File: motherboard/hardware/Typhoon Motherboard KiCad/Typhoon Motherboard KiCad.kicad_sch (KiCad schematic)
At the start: 2 parts, among them P1 USB_C_Plug_USB2.0, U1 ESP32-S3-WROOM-1

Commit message: added most recent motherboard files
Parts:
- added R1, R2: 22, symbol Device:R_US
- added U2: CP2102N-Axx-xQFN20, Package_DFN_QFN:SiliconLabs_QFN-20-1EP_3x3mm_P0.5mm, symbol Interface_USB:CP2102N-Axx-xQFN20
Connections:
- net GND: now reaches U1.1 (GND), U1.40 (GND), U1.41 (GND)
- net GND: now also P1.A1 (GND), P1.A12 (GND), P1.B1 (GND), P1.B12 (GND)
- net +3.3V: now reaches U1.2 (3V3)
- net at U1.36 (RXD0): now also U2.17 (RXD)
- net at U1.37 (TXD0): now also U2.18 (TXD)
- net +5V: now reaches P1.A4 (VBUS), P1.A9 (VBUS), P1.B4 (VBUS), P1.B9 (VBUS)
- net at P1.A6 (D+): now also R2.1
- net at P1.A7 (D-): now also R1.1
- new net: R1.2, U2.5 (D-)
- new net: R2.2, U2.4 (D+)
- new net: U2.12 (GND), U2.21 (GND), U2.3 (GND)
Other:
- note added: "3.3V"
- moved on the sheet: P1

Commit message: Minor Changes
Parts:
- added J1: Conn_01x01_Pin, symbol Connector:Conn_01x01_Pin
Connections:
- net +3.3V: no longer names the net of U1.2 (3V3)
- net +3.3V: now also J1.1 (Pin_1)
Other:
- note removed: "3.3V"
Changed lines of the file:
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@@
+	(wire
+		(pts
+			(xy 194.31 50.8) (xy 194.31 59.69)
+		)
+		(stroke
+			(width 0)
+			(type default)
+		)
+	)
 	(wire
 		(pts
@@
 			(width 0)
 			(type default)
-		)
-	)
-	(text "3.3V"
-		(exclude_from_sim no)
-		(at 189.992 56.134 0)
-		(effects
-			(font
-				(size 1.27 1.27)
-			)
 		)
 	)
@@
 	)
 	(symbol
-		(lib_id "power:+3.3V")
-		(at 194.31 59.69 0)
-		(unit 1)
-		(exclude_from_sim no)
-		(in_bom yes)
-		(on_board yes)
-		(dnp no)
-		(fields_autoplaced yes)
-		(property "Reference" "#PWR01"
-			(at 194.31 63.5 0)
-			(effects
-				(font
-					(size 1.27 1.27)
-				)
-				(hide yes)
-			)
-		)
-		(property "Value" "+3.3V"
-			(at 194.31 54.61 0)
-			(effects
-				(font
-					(size 1.27 1.27)
-				)
-			)
-		)
-		(property "Footprint" ""
-			(at 194.31 59.69 0)
-			(effects
-				(font
-					(size 1.27 1.27)
-				)
-				(hide yes)
-			)
-		)
-		(property "Datasheet" ""
-			(at 194.31 59.69 0)
-			(effects
-				(font
-					(size 1.27 1.27)
-				)
-				(hide yes)
-			)
-		)
-		(property "Description" "Power symbol creates a global label with name \"+3.3V\""
-			(at 194.31 59.69 0)
-			(effects
-				(font
-					(size 1.27 1.27)
-				)
-				(hide yes)
-			)
-		)
-		(pin "1"
-		)
-		(instances
-			(project "Typhoon Motherboard KiCad"
-				(path "/13012fcd-02e9-4b82-8301-52da00f60a6e"
-					(reference "#PWR01")
-					(unit 1)
-				)
-			)
-		)
-	)
-	(symbol
 		(lib_id "power:GND")
 		(at 97.79 104.14 0)
@@
 					(unit 1)
 				)
+			)
+		)
+	)
+	(symbol
+		(lib_id "Connector:Conn_01x01_Pin")
+		(at 189.23 50.8 0)
+		(unit 1)
+		(exclude_from_sim no)
+		(in_bom yes)
+		(on_board yes)
+		(dnp no)
+		(fields_autoplaced yes)
+		(property "Reference" "J1"
+			(at 189.865 45.72 0)
+			(effects
+				(font
+					(size 1.27 1.27)
+				)
+			)
+		)
+		(property "Value" "Conn_01x01_Pin"
+			(at 189.865 48.26 0)
+			(effects
+				(font
+					(size 1.27 1.27)
+				)
+			)
+		)
+		(property "Footprint" ""
+			(at 189.23 50.8 0)
+			(effects
+				(font
+					(size 1.27 1.27)
+				)
+				(hide yes)
+			)
+		)
+		(property "Datasheet" "~"
+			(at 189.23 50.8 0)
+			(effects
+				(font
+					(size 1.27 1.27)
+				)
+				(hide yes)
+			)
+		)
+		(property "Description" "Generic connector, single row, 01x01, script generated"
+			(at 189.23 50.8 0)
+			(effects
+				(font
+					(size 1.27 1.27)
+				)
+				(hide yes)
+			)
+		)
+		(pin "1"
+		)
+		(instances
+			(project "Typhoon Motherboard KiCad"
+				(path "/13012fcd-02e9-4b82-8301-52da00f60a6e"
+					(reference "J1")
+					(unit 1)
+				)

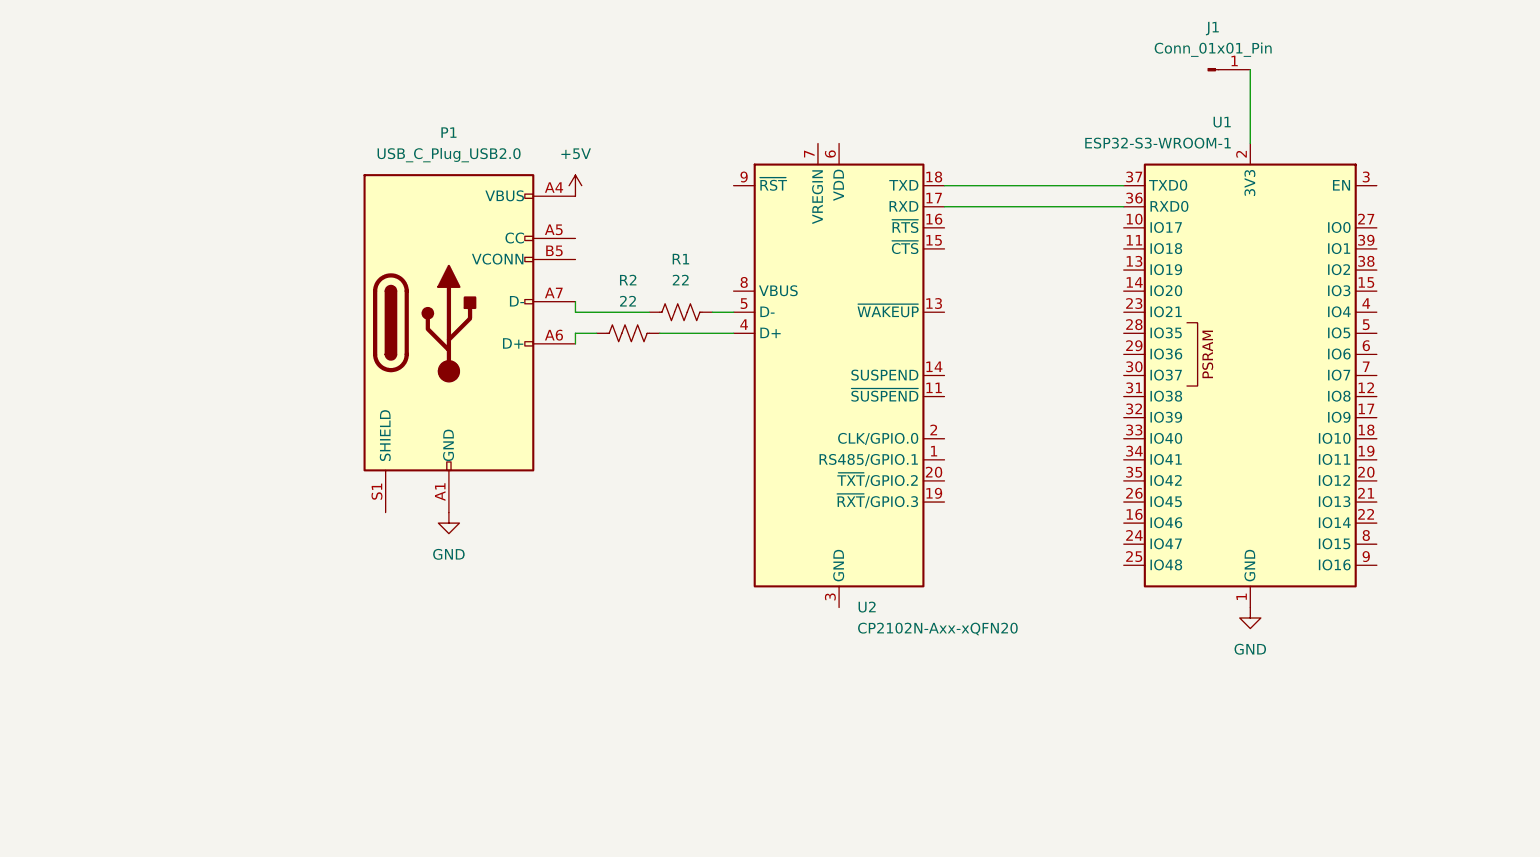
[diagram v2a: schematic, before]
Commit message: Removed  UART
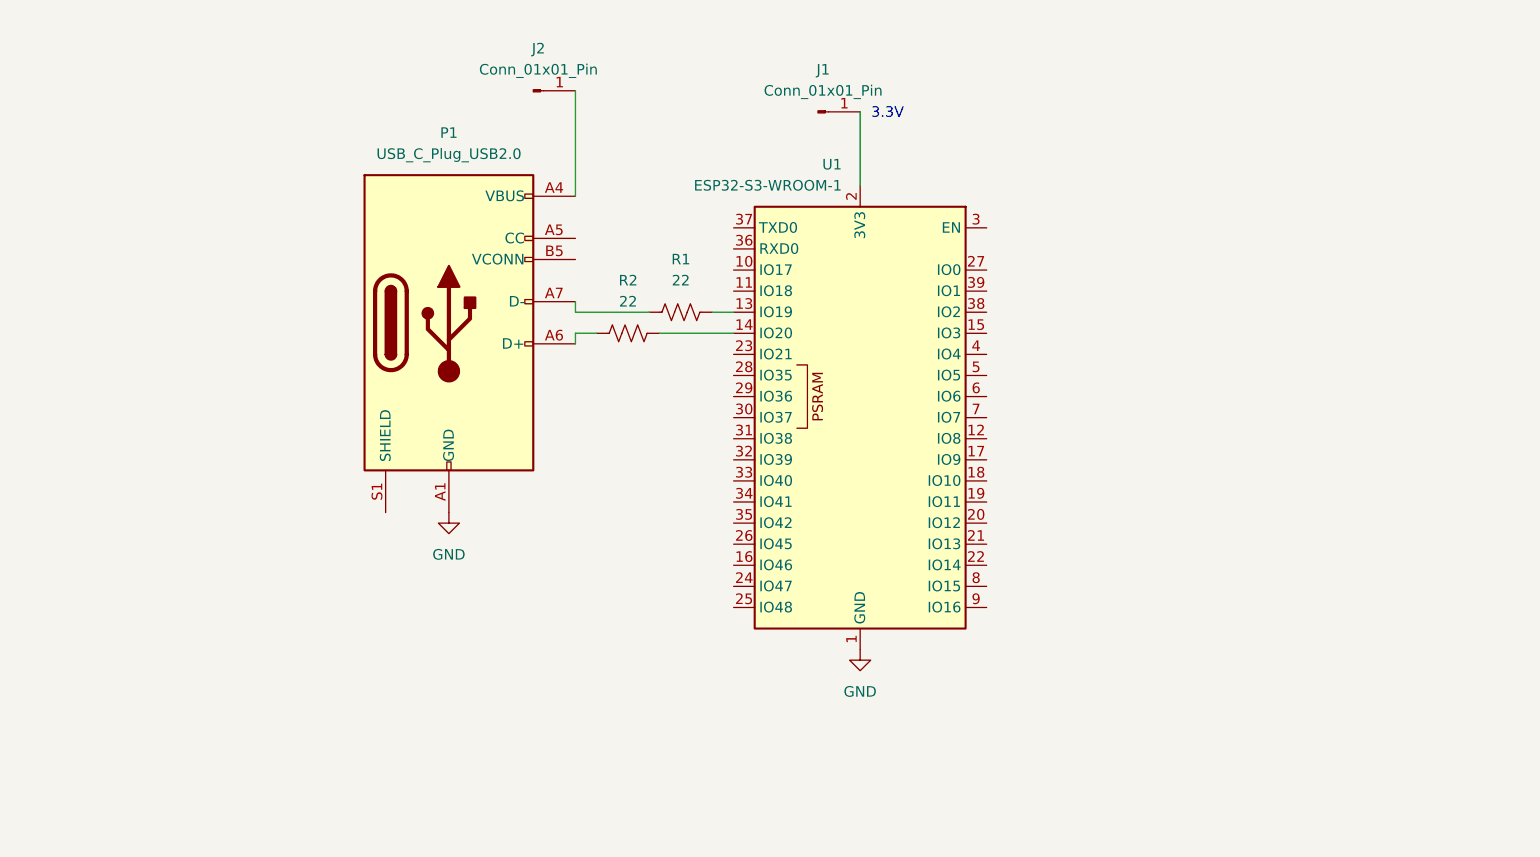
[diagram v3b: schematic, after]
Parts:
- removed U2: CP2102N-Axx-xQFN20, Package_DFN_QFN:SiliconLabs_QFN-20-1EP_3x3mm_P0.5mm, symbol Interface_USB:CP2102N-Axx-xQFN20
- added J2: Conn_01x01_Pin, symbol Connector:Conn_01x01_Pin
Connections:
- net at R1.2: now also U1.13 (IO19)
- net at R2.2: now also U1.14 (IO20)
- net +5V: no longer names the net of P1.A4 (VBUS), P1.A9 (VBUS), P1.B4 (VBUS), P1.B9 (VBUS)
- net +5V: now also J2.1 (Pin_1)
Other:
- note added: "3.3V"
- moved on the sheet: J1, U1
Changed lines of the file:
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@@
 	(wire
 		(pts
-			(xy 194.31 50.8) (xy 194.31 59.69)
-		)
-		(stroke
-			(width 0)
-			(type default)
-		)
-	)
-	(wire
-		(pts
-			(xy 179.07 64.77) (xy 157.48 64.77)
+			(xy 147.32 55.88) (xy 147.32 64.77)
+		)
+		(stroke
+			(width 0)
+			(type default)
+		)
+	)
+	(wire
+		(pts
+			(xy 113.03 53.34) (xy 113.03 66.04)
 		)
 		(stroke
@@
 	(wire
 		(pts
-			(xy 179.07 67.31) (xy 157.48 67.31)
-		)
-		(stroke
-			(width 0)
-			(type default)
-		)
-	)
-	(wire
-		(pts
 			(xy 132.08 80.01) (xy 129.54 80.01)
 		)
@@
 			(width 0)
 			(type default)
+		)
+	)
+	(text "3.3V"
+		(exclude_from_sim no)
+		(at 150.622 56.134 0)
+		(effects
+			(font
+				(size 1.27 1.27)
+			)
+		)
+	)
+	(symbol
+		(lib_id "Connector:Conn_01x01_Pin")
+		(at 107.95 53.34 0)
+		(unit 1)
+		(exclude_from_sim no)
+		(in_bom yes)
+		(on_board yes)
+		(dnp no)
+		(fields_autoplaced yes)
+		(property "Reference" "J2"
+			(at 108.585 48.26 0)
+			(effects
+				(font
+					(size 1.27 1.27)
+				)
+			)
+		)
+		(property "Value" "Conn_01x01_Pin"
+			(at 108.585 50.8 0)
+			(effects
+				(font
+					(size 1.27 1.27)
+				)
+			)
+		)
+		(property "Footprint" ""
+			(at 107.95 53.34 0)
+			(effects
+				(font
+					(size 1.27 1.27)
+				)
+				(hide yes)
+			)
+		)
+		(property "Datasheet" "~"
+			(at 107.95 53.34 0)
+			(effects
+				(font
+					(size 1.27 1.27)
+				)
+				(hide yes)
+			)
+		)
+		(property "Description" "Generic connector, single row, 01x01, script generated"
+			(at 107.95 53.34 0)
+			(effects
+				(font
+					(size 1.27 1.27)
+				)
+				(hide yes)
+			)
+		)
+		(pin "1"
+		)
+		(instances
+			(project "Typhoon Motherboard KiCad"
+				(path "/13012fcd-02e9-4b82-8301-52da00f60a6e"
+					(reference "J2")
+					(unit 1)
+				)
+			)
 		)
 	)
@@
 	(symbol
 		(lib_id "RF_Module:ESP32-S3-WROOM-1")
-		(at 194.31 87.63 0)
+		(at 147.32 92.71 0)
 		(mirror y)
 		(unit 1)
@@
 		(dnp no)
 		(property "Reference" "U1"
-			(at 192.1159 57.15 0)
+			(at 145.1259 62.23 0)
 			(effects
 				(font
@@
 		)
 		(property "Value" "ESP32-S3-WROOM-1"
-			(at 192.1159 59.69 0)
+			(at 145.1259 64.77 0)
 			(effects
 				(font
@@
 		)
 		(property "Footprint" "RF_Module:ESP32-S3-WROOM-1"
-			(at 194.31 85.09 0)
+			(at 147.32 90.17 0)
 			(effects
 				(font
@@
 		)
 		(property "Datasheet" "https://www.espressif.com/sites/default/files/documentation/esp32-s3-wroom-1_wroom-1u_datasheet_en.pdf"
-			(at 194.31 87.63 0)
+			(at 147.32 92.71 0)
 			(effects
 				(font
@@
 		)
 		(property "Description" "RF Module, ESP32-S3 SoC, Wi-Fi 802.11b/g/n, Bluetooth, BLE, 32-bit, 3.3V, onboard antenna, SMD"
-			(at 194.31 87.63 0)
+			(at 147.32 92.71 0)
 			(effects
 				(font
@@
 	(symbol
 		(lib_id "power:GND")
-		(at 194.31 115.57 0)
+		(at 147.32 120.65 0)
 		(unit 1)
 		(exclude_from_sim no)
@@
 		(fields_autoplaced yes)
 		(property "Reference" "#PWR04"
-			(at 194.31 121.92 0)
+			(at 147.32 127 0)
 			(effects
 				(font
@@
 		)
 		(property "Value" "GND"
-			(at 194.31 120.65 0)
+			(at 147.32 125.73 0)
 			(effects
 				(font
@@
 		)
 		(property "Footprint" ""
-			(at 194.31 115.57 0)
+			(at 147.32 120.65 0)
 			(effects
 				(font
@@
 		)
 		(property "Datasheet" ""
-			(at 194.31 115.57 0)
+			(at 147.32 120.65 0)
 			(effects
 				(font
@@
 		)
 		(property "Description" "Power symbol creates a global label with name \"GND\" , ground"
-			(at 194.31 115.57 0)
+			(at 147.32 120.65 0)
 			(effects
 				(font
@@
 	)
 	(symbol
-		(lib_id "power:+5V")
-		(at 113.03 66.04 0)
-		(unit 1)
-		(exclude_from_sim no)
-		(in_bom yes)
-		(on_board yes)
-		(dnp no)
-		(property "Reference" "#PWR02"
-			(at 113.03 69.85 0)
-			(effects
-				(font
-					(size 1.27 1.27)
-				)
-				(hide yes)
-			)
-		)
-		(property "Value" "+5V"
-			(at 113.03 60.96 0)
-			(effects
-				(font
-					(size 1.27 1.27)
-				)
-			)
-		)
-		(property "Footprint" ""
-			(at 113.03 66.04 0)
-			(effects
-				(font
-					(size 1.27 1.27)
-				)
-				(hide yes)
-			)
-		)
-		(property "Datasheet" ""
-			(at 113.03 66.04 0)
-			(effects
-				(font
-					(size 1.27 1.27)
-				)
-				(hide yes)
-			)
-		)
-		(property "Description" "Power symbol creates a global label with name \"+5V\""
-			(at 113.03 66.04 0)
-			(effects
-				(font
-					(size 1.27 1.27)
-				)
-				(hide yes)
-			)
-		)
-		(pin "1"
-		)
-		(instances
-			(project "Typhoon Motherboard KiCad"
-				(path "/13012fcd-02e9-4b82-8301-52da00f60a6e"
-					(reference "#PWR02")
-					(unit 1)
-				)
-			)
-		)
-	)
-	(symbol
 		(lib_id "power:GND")
 		(at 97.79 104.14 0)
@@
 	)
 	(symbol
-		(lib_id "Interface_USB:CP2102N-Axx-xQFN20")
-		(at 144.78 87.63 0)
-		(unit 1)
-		(exclude_from_sim no)
-		(in_bom yes)
-		(on_board yes)
-		(dnp no)
-		(fields_autoplaced yes)
-		(property "Reference" "U2"
-			(at 146.9741 115.57 0)
-			(effects
-				(font
-					(size 1.27 1.27)
-				)
-				(justify left)
-			)
-		)
-		(property "Value" "CP2102N-Axx-xQFN20"
-			(at 146.9741 118.11 0)
-			(effects
-				(font
-					(size 1.27 1.27)
-				)
-				(justify left)
-			)
-		)
-		(property "Footprint" "Package_DFN_QFN:SiliconLabs_QFN-20-1EP_3x3mm_P0.5mm"
-			(at 176.53 114.3 0)
-			(effects
-				(font
-					(size 1.27 1.27)
-				)
-				(hide yes)
-			)
-		)
-		(property "Datasheet" "https://www.silabs.com/documents/public/data-sheets/cp2102n-datasheet.pdf"
-			(at 146.05 106.68 0)
-			(effects
-				(font
-					(size 1.27 1.27)
-				)
-				(hide yes)
-			)
-		)
-		(property "Description" "USB to UART master bridge, QFN-20"
-			(at 144.78 87.63 0)
-			(effects
-				(font
-					(size 1.27 1.27)
-				)
-				(hide yes)
-			)
-		)
-		(pin "1"
-		)
-		(pin "14"
-		)
-		(pin "15"
-		)
-		(pin "10"
-		)
-		(pin "11"
-		)
-		(pin "4"
-		)
-		(pin "5"
-		)
-		(pin "6"
-		)
-		(pin "21"
-		)
-		(pin "3"
-		)
-		(pin "16"
-		)
-		(pin "17"
-		)
-		(pin "18"
-		)
-		(pin "19"
-		)
-		(pin "7"
-		)
-		(pin "8"
-		)
-		(pin "9"
-		)
-		(pin "12"
-		)
-		(pin "13"
-		)
-		(pin "2"
-		)
-		(pin "20"
-		)
-		(instances
-			(project "Typhoon Motherboard KiCad"
-				(path "/13012fcd-02e9-4b82-8301-52da00f60a6e"
-					(reference "U2")
-					(unit 1)
-				)
-			)
-		)
-	)
-	(symbol
 		(lib_id "Connector:Conn_01x01_Pin")
-		(at 189.23 50.8 0)
+		(at 142.24 55.88 0)
 		(unit 1)
 		(exclude_from_sim no)
@@
 		(fields_autoplaced yes)
 		(property "Reference" "J1"
-			(at 189.865 45.72 0)
+			(at 142.875 50.8 0)
 			(effects
 				(font
@@
 		)
 		(property "Value" "Conn_01x01_Pin"
-			(at 189.865 48.26 0)
+			(at 142.875 53.34 0)
 			(effects
 				(font
@@
 		)
 		(property "Footprint" ""
-			(at 189.23 50.8 0)
+			(at 142.24 55.88 0)
 			(effects
 				(font
@@
 		)
 		(property "Datasheet" "~"
-			(at 189.23 50.8 0)
+			(at 142.24 55.88 0)
 			(effects
 				(font
@@
 		)
 		(property "Description" "Generic connector, single row, 01x01, script generated"
-			(at 189.23 50.8 0)
-			(effects
-				(font
+			(at 142.24 55.88 0)
+			(effects
+				(font
